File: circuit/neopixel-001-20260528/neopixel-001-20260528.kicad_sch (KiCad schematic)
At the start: 60 parts, among them J1 Conn_NeoPixel, P1 ESP32C3_{1}, P10 unitV3, P11 unitV4, P12 unitV4, P2 ESP32C3_{1}, P3 ESP32C3_{2}, P4 ESP32C3_{2}, P5 unitV1, P6 unitV1, P7 unitV2, P8 unitV2, P9 unitV3, SW1 SW_SPST, SW2 SW_SPST, SW3 SW_SPST, SW4 SW_SPST, U1 SSD1306

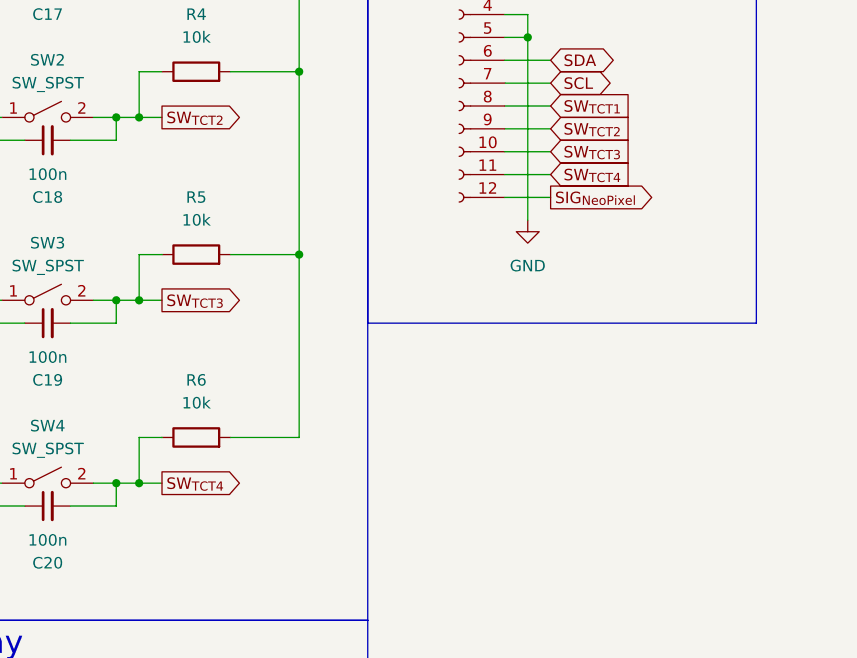
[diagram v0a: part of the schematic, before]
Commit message: Update サブ基板とネオピク基板のラベル名を統一・回路図PDFを作成
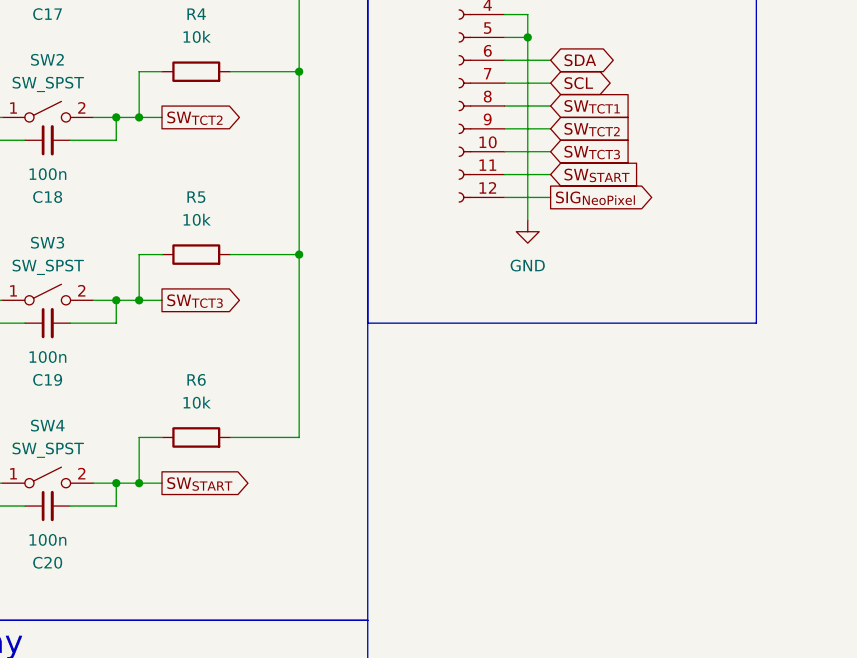
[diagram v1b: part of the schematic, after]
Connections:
- net SW_{TCT4} renamed SW_{START}
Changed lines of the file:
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@@
 		)
 	)
-	(global_label "SW_{TCT4}"
+	(global_label "SW_{START}"
 		(shape output)
 		(at 144.78 90.17 0)
@@
 		)
 		(property "Intersheetrefs" "${INTERSHEET_REFS}"
-			(at 156.776 90.17 0)
+			(at 154.0282 90.17 0)
 			(hide yes)
 			(show_name no)
@@
 		)
 	)
-	(global_label "SW_{TCT4}"
+	(global_label "SW_{START}"
 		(shape input)
 		(at 187.96 55.88 0)
@@
 		)
 		(property "Intersheetrefs" "${INTERSHEET_REFS}"
-			(at 199.7144 55.88 0)
+			(at 197.2082 55.88 0)
 			(hide yes)
 			(show_name no)

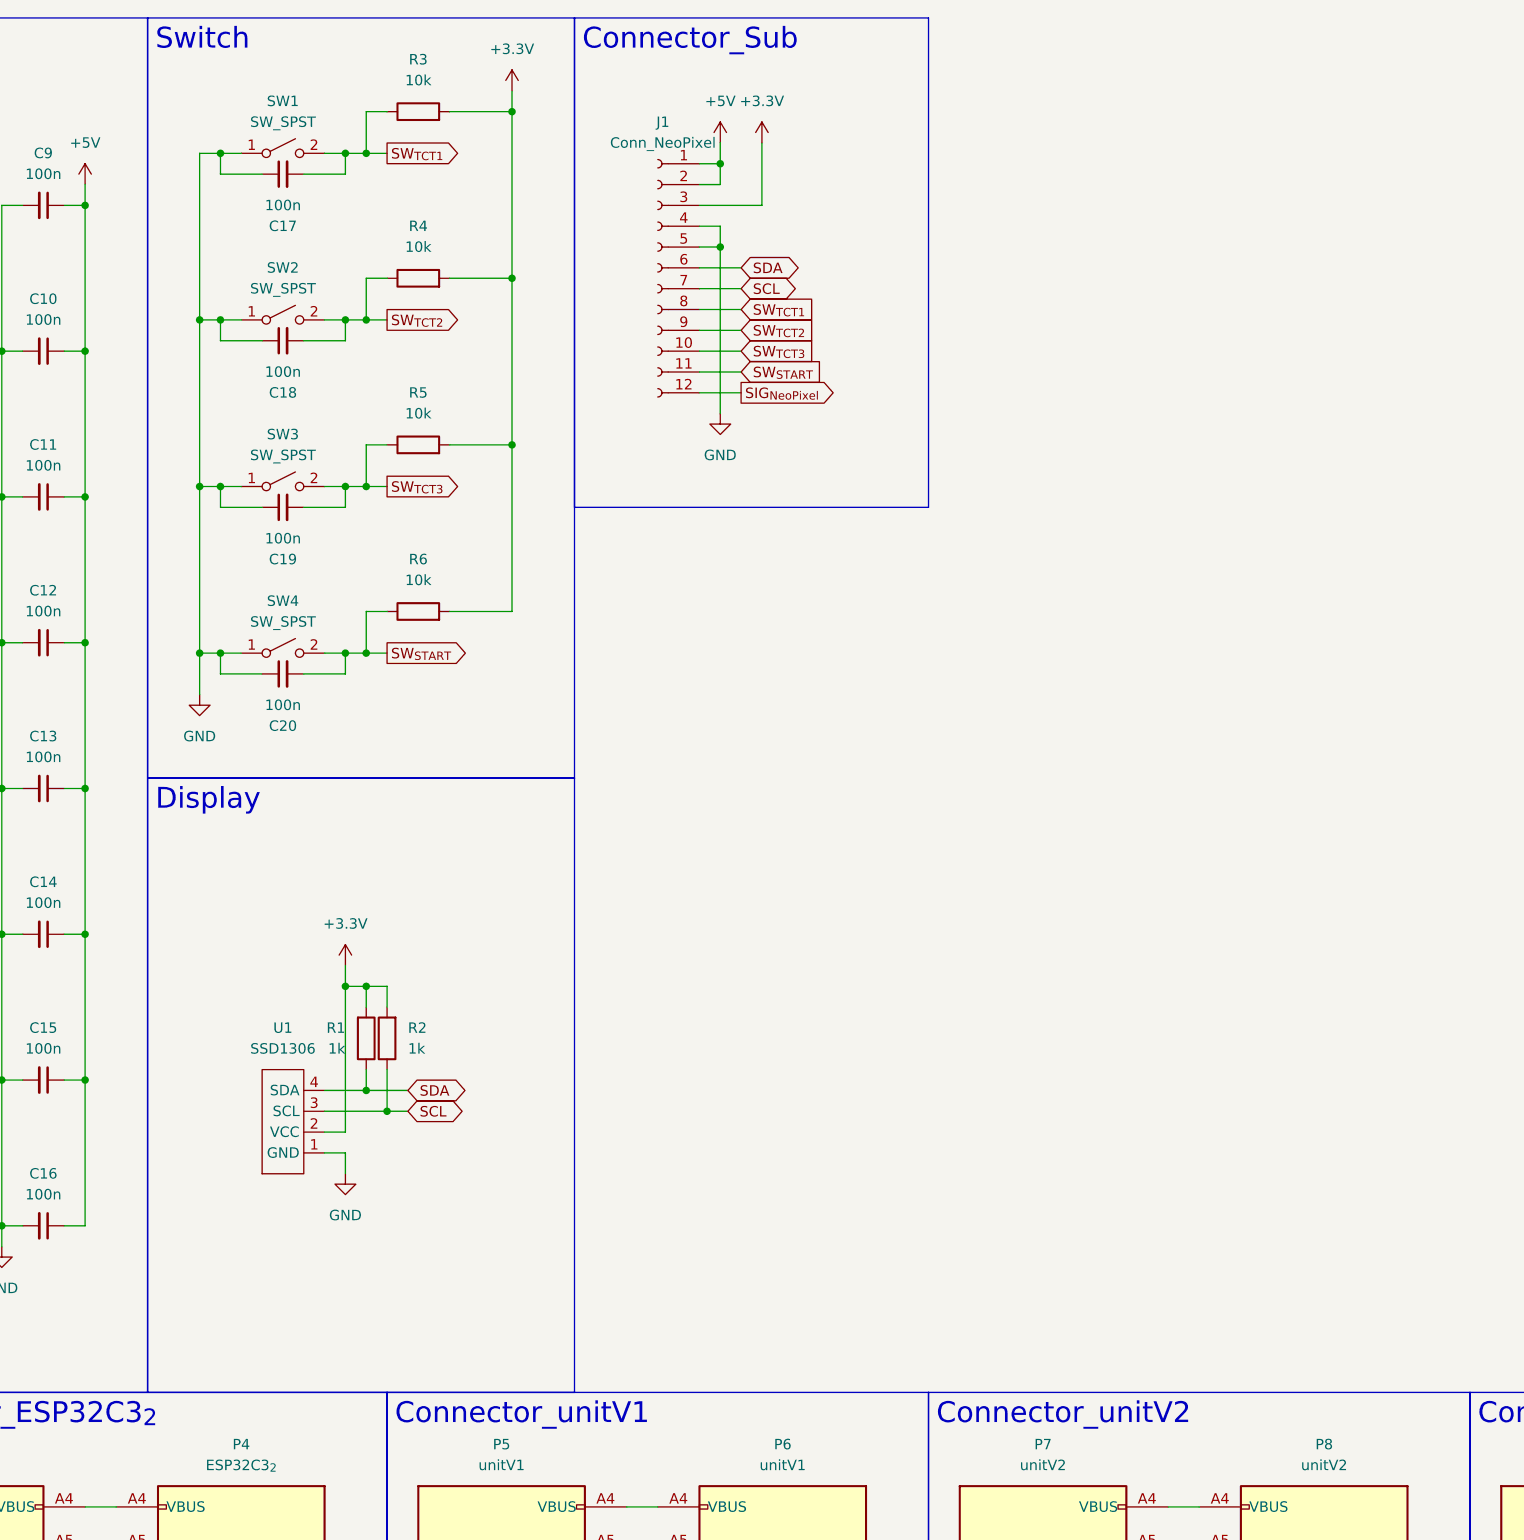
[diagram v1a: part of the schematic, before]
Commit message: Update ネオピク基板の回路図とSWLEDのフットプリントを更新
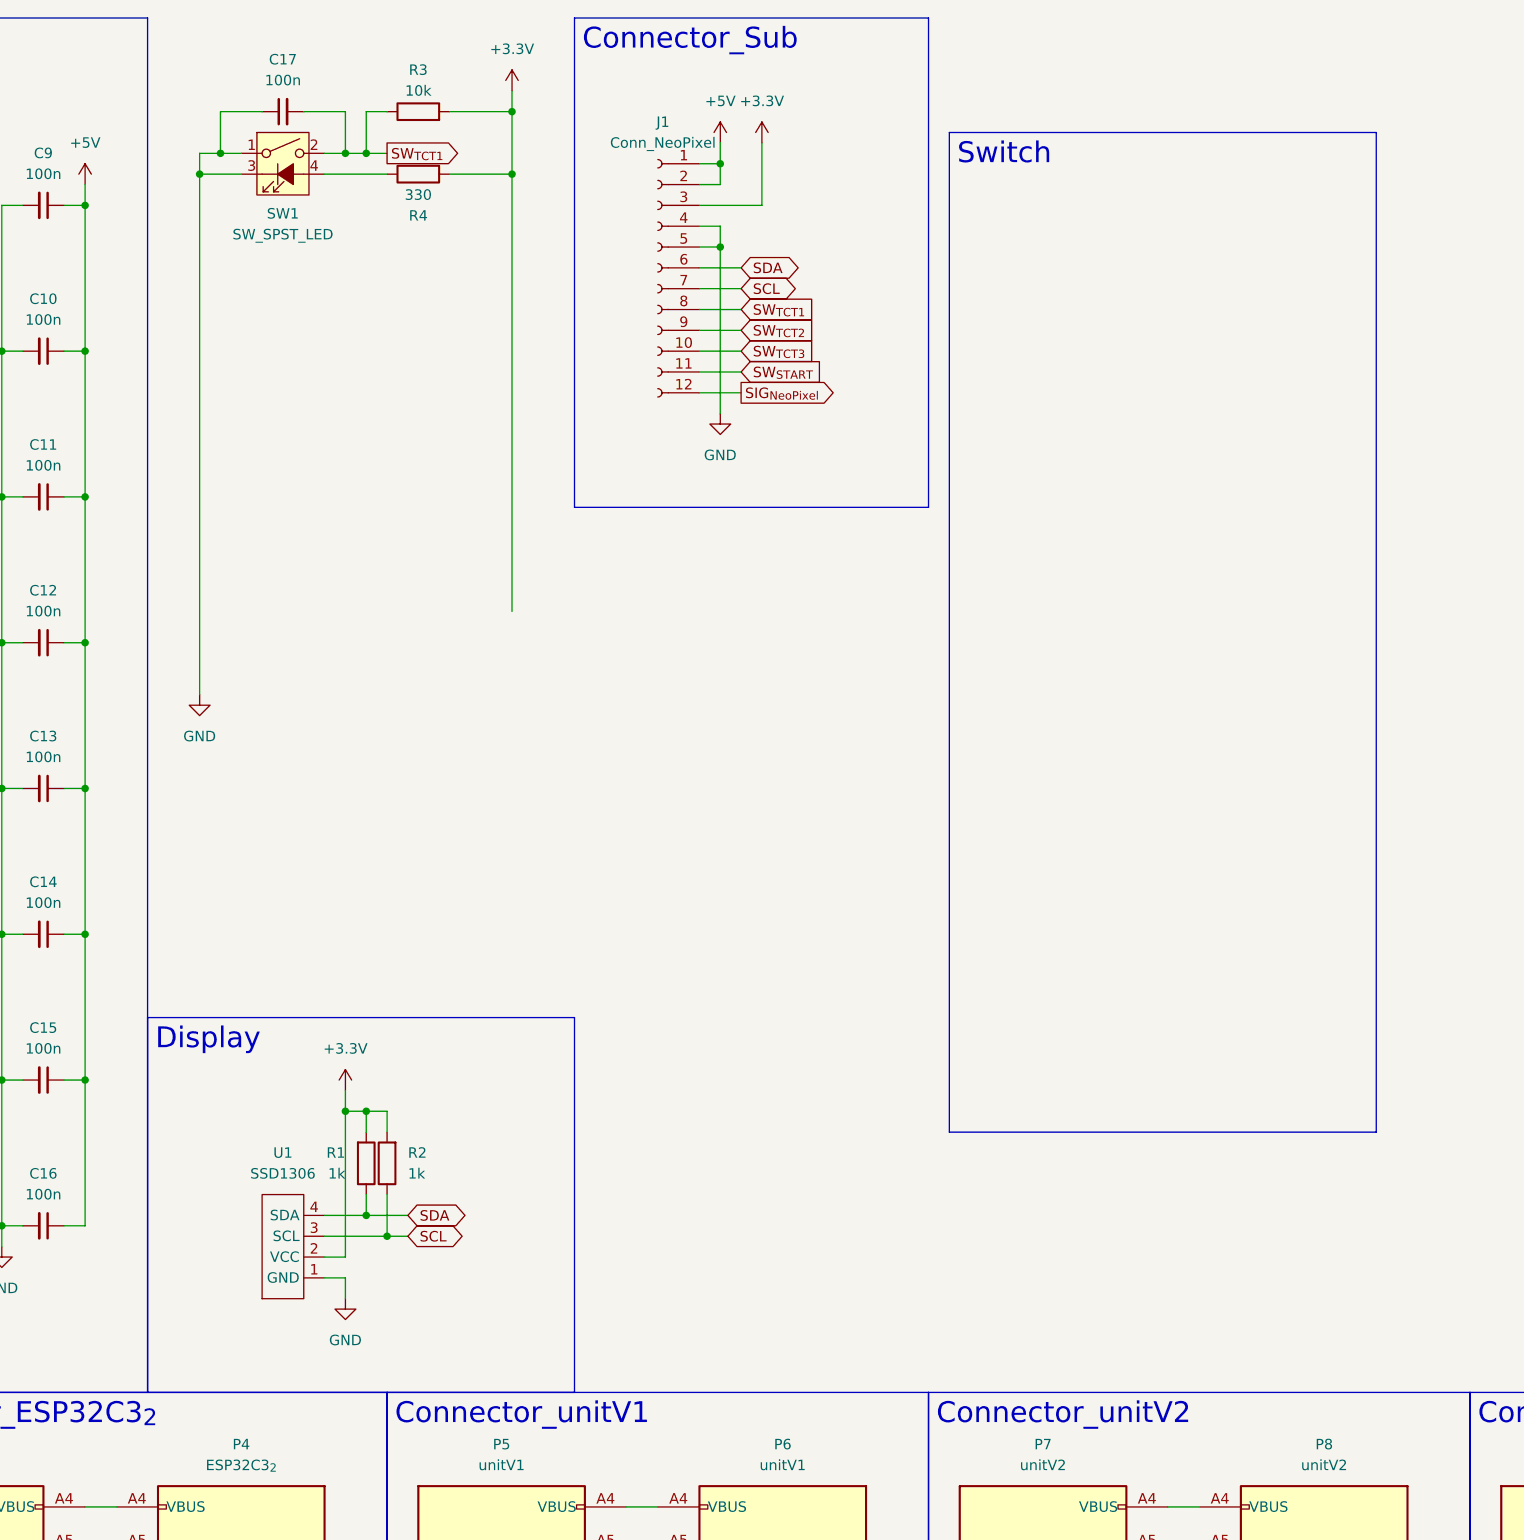
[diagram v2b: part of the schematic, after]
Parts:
- removed C18, C19, C20: 100n, Capacitor_SMD:C_0805_2012Metric, symbol Device:C_Small
- removed R5, R6: 10k, Resistor_SMD:R_0805_2012Metric, symbol Device:R
- removed SW1, SW2, SW3, SW4: SW_SPST, @Thrive_footprint_neopixel:ST-12-401FC-G, symbol Switch:SW_SPST
- added SW1: SW_SPST_LED, symbol Switch:SW_SPST_LED
- R4: value 10k -> 330
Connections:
- net GND: now also SW1.1, SW1.3 (K)
- net SW_{TCT1}: now also SW1.2
- net SW_{TCT2}: no longer R4.1
- new net: R4.1, SW1.4 (A)
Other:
- moved on the sheet: C17, R1, R2, R4, U1

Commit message: Update ネオピクセル基板の回路図を更新
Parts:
- added C18, C19, C20: 100n, Capacitor_SMD:C_0805_2012Metric, symbol Device:C_Small
- added R10, R6, R8: 330, Resistor_SMD:R_0805_2012Metric, symbol Device:R
- added R5, R7, R9: 10k, Resistor_SMD:R_0805_2012Metric, symbol Device:R
- added SW2, SW3, SW4: SW_SPST_LED, symbol Switch:SW_SPST_LED
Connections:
- net +3.3V: now also R10.2, R5.2, R6.2, R7.2, R8.2, R9.2
- net GND: now also C18.1, C19.1, C20.1, SW2.1, SW2.3 (K), SW3.1, SW3.3 (K), SW4.1, SW4.3 (K)
- net SW_{TCT1}: now also C18.2, C19.2, C20.2, R5.1, R7.1, R9.1, SW2.2, SW3.2, SW4.2
- new net: R8.1, SW3.4 (A)
- new net: R6.1, SW2.4 (A)
- new net: R10.1, SW4.4 (A)
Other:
- moved on the sheet: R4

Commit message: Update ネオピク基板の回路図とREADMEを更新
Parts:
- added J2, J3: Conn_01x02_Pin, symbol Connector:Conn_01x02_Pin
- added MES1: Voltmeter_DC, symbol Device:Voltmeter_DC
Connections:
- net GND: now also J2.2 (Pin_2), J3.2 (Pin_2), MES1.1 (-)
- new net +48V: J2.1 (Pin_1), J3.1 (Pin_1), MES1.2 (+)
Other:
- moved on the sheet: C1, C10, C11, C12, C13, C14, C15, C16, C17, C18, C19, C2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

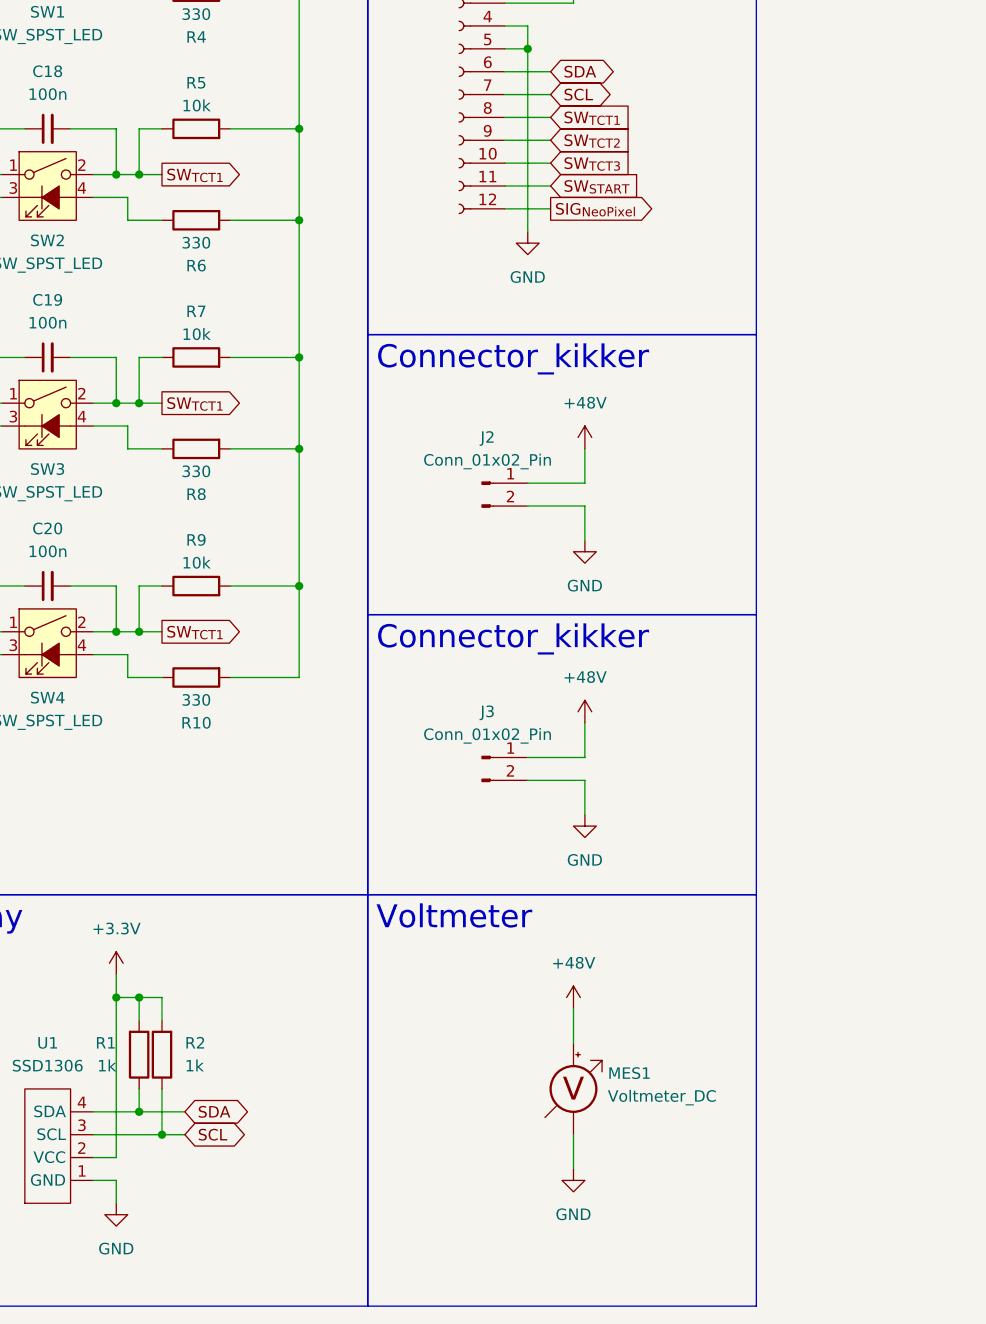
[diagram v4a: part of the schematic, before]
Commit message: Update ネオピクセル基板の回路図完成した
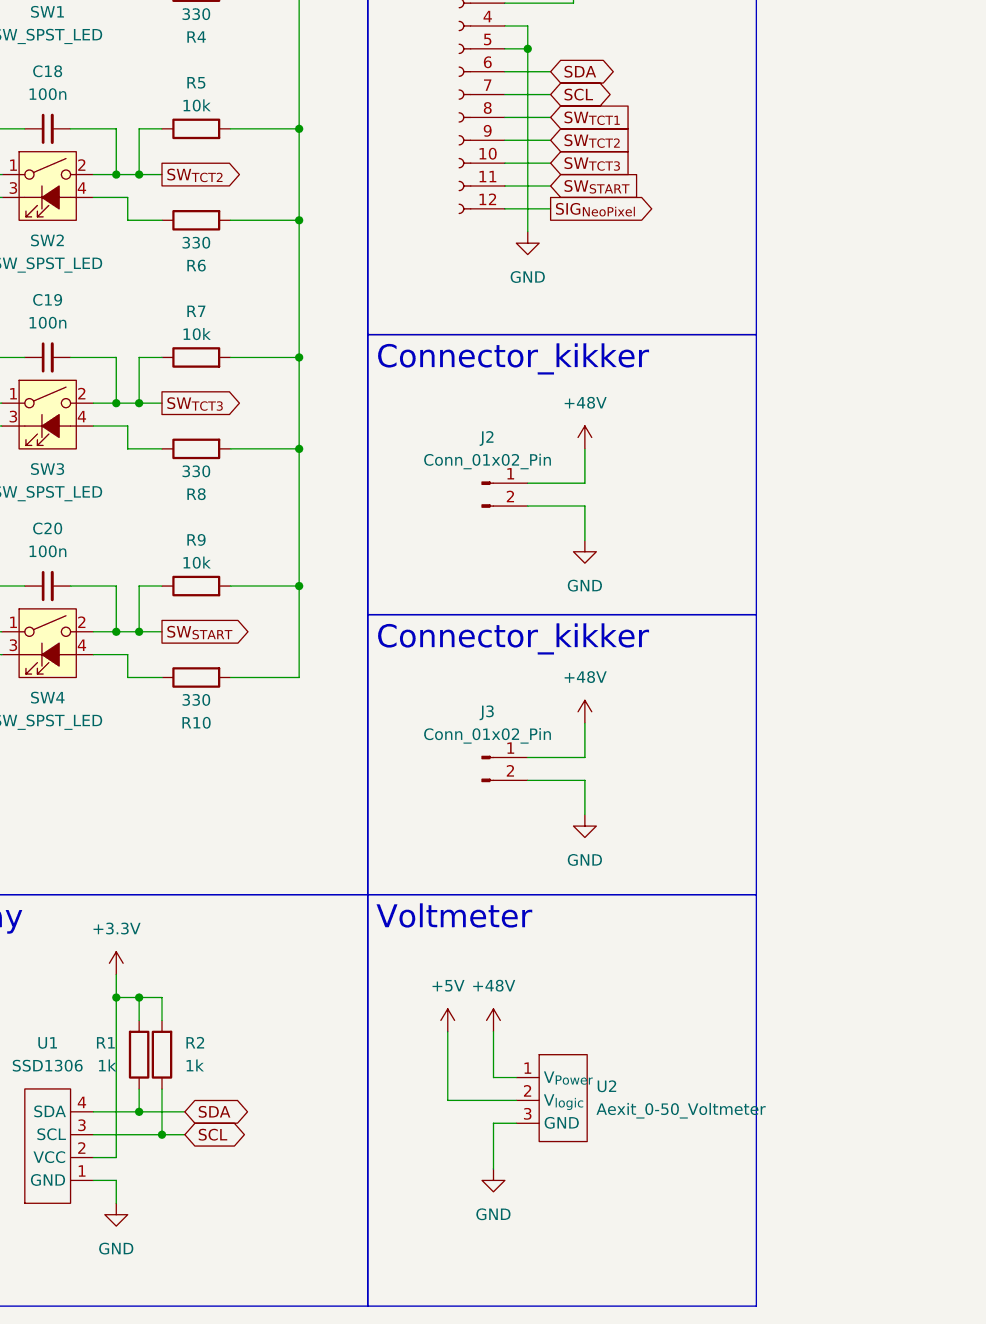
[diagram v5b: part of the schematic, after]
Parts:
- removed MES1: Voltmeter_DC, symbol Device:Voltmeter_DC
- added U2: Aexit_0-50_Voltmeter, @Thrive_footprint_neopixel:Aexit_0-50_Voltmeter, symbol @Thrive_symbol_neopixel:Aexit_0-50_Voltmeter
- J2, J3: footprint (none) -> Connector_JST:JST_XH_B2B-XH-A_1x02_P2.50mm_Vertical
- P10, P12, P2, P4, P6, P8: footprint (none) -> @Thrive_footprint_neopixel:USB_Type-C_Vertical_ C6332304
- SW1, SW2, SW3, SW4: footprint (none) -> @Thrive_footprint_neopixel:ST-12-401FC-G
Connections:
- net +48V: now also U2.1 (V_{Power})
- net +5V: now also U2.2 (V_{logic})
- net GND: now also U2.3 (GND)
- net SW_{START}: now also C20.2, R9.1, SW4.2
- net SW_{TCT1}: no longer C18.2, C19.2, C20.2, R5.1, R7.1, R9.1, SW2.2, SW3.2, SW4.2
- net SW_{TCT2}: now also C18.2, R5.1, SW2.2
- net SW_{TCT3}: now also C19.2, R7.1, SW3.2
